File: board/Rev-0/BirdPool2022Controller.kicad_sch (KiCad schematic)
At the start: 28 parts, among them J1 ISP, J2 OSTVN02A150, J3 OSTVN04A150, J4 OSTVN02A150, J5 OSTVN04A150, J6 Conn_01x06, K1 G5LE-14_DC5, U1 PC817, U3 PIC18F1330

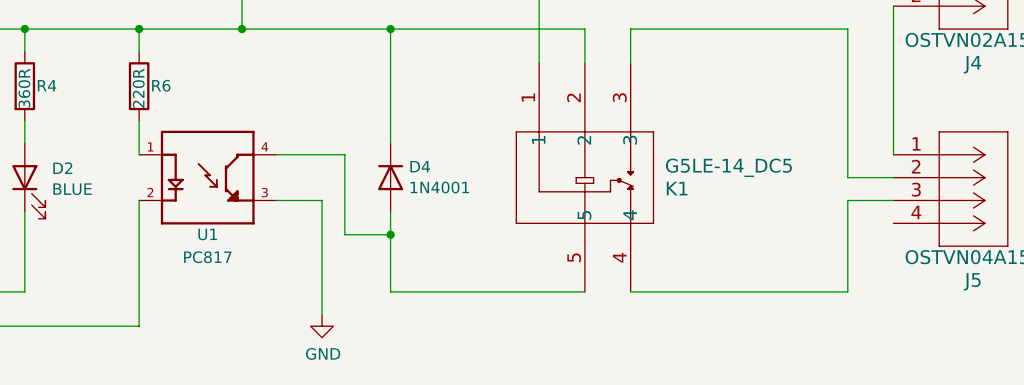
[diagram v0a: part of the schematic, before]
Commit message: Add a note for Rev-0 board
-Add the following note for the Rev-0 board: "PC817 is not efficient enough for current required for the relay. I used instead of Darlington one, the PS2533-1-V-A. Digi-Key 559-1255-ND>.
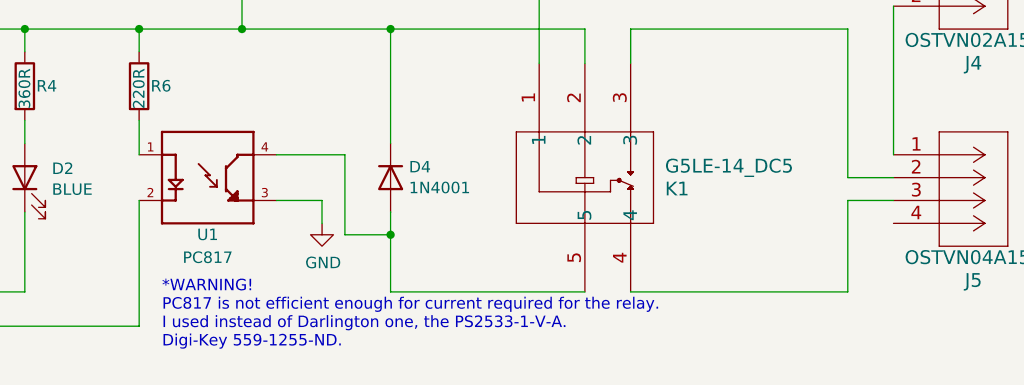
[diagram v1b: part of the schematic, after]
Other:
- note added: "*WARNING! PC817 is not efficient enough for current required for the relay. I used instead of Darlington one, the PS2533-1-V-A. Digi-Key 559-1255-ND."
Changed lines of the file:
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@@
+    (stroke (width 0) (type default) (color 0 0 0 0))
+  )
+  (wire (pts (xy 93.98 176.53) (xy 93.98 179.07))
     (stroke (width 0) (type default) (color 0 0 0 0))
   )
@@
     (stroke (width 0) (type default) (color 0 0 0 0))
   )
-  (wire (pts (xy 93.98 176.53) (xy 93.98 189.23))
-    (stroke (width 0) (type default) (color 0 0 0 0))
-  )
   (wire (pts (xy 269.24 106.68) (xy 269.24 109.22))
     (stroke (width 0) (type default) (color 0 0 0 0))
@@
   (wire (pts (xy 87.63 88.9) (xy 77.47 88.9))
     (stroke (width 0) (type default) (color 0 0 0 0))
+  )
+  (text "*WARNING!\nPC817 is not efficient enough for current required for the relay.\nI used instead of Darlington one, the PS2533-1-V-A.\nDigi-Key 559-1255-ND."
+    (at 76.2 193.04 0)
+    (effects (font (size 1.27 1.27)) (justify left bottom))
   )
   (label "PGD" (at 20.32 88.9 180)
@@
     (pin "5")
   )
-  (symbol (lib_id "power:GND") (at 93.98 189.23 0) (unit 1)
-    (in_bom yes) (on_board yes)
-    (property "Reference" "#PWR08" (id 0) (at 93.98 195.58 0)
-      (effects (font (size 1.27 1.27)) hide)
-    )
-    (property "Value" "GND" (id 1) (at 94.107 193.6242 0))
-    (property "Footprint" "" (id 2) (at 93.98 189.23 0)
-      (effects (font (size 1.27 1.27)) hide)
-    )
-    (property "Datasheet" "" (id 3) (at 93.98 189.23 0)
-      (effects (font (size 1.27 1.27)) hide)
-    )
+  (symbol (lib_id "power:GND") (at 93.98 179.07 0) (unit 1)
+    (in_bom yes) (on_board yes)
+    (property "Reference" "#PWR08" (id 0) (at 93.98 185.42 0)
+      (effects (font (size 1.27 1.27)) hide)
+    )
+    (property "Value" "GND" (id 1) (at 94.107 183.4642 0))
+    (property "Footprint" "" (id 2) (at 93.98 179.07 0)
+      (effects (font (size 1.27 1.27)) hide)
+    )
+    (property "Datasheet" "" (id 3) (at 93.98 179.07 0)
+      (effects (font (size 1.27 1.27)) hide)
+    )
